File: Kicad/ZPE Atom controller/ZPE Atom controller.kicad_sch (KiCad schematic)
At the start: 44 parts, among them IC1 TC4424AVPA, J1 50 ohm 21 turns, P1 CONN_01X18, P2 CONN_01X18, Q1 2N2222, Q2 IRF3205, SW1 ON/OFF, SW2 SW_SPST, SW3 SW_SPST, SW4 SW_SPST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

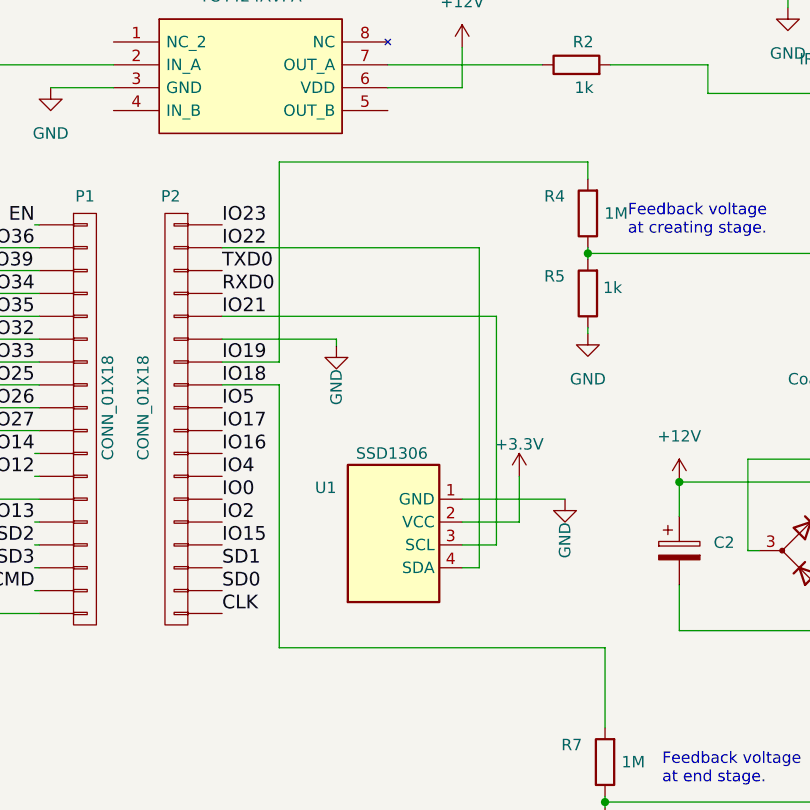
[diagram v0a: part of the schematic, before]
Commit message: Fixed analog read pin input
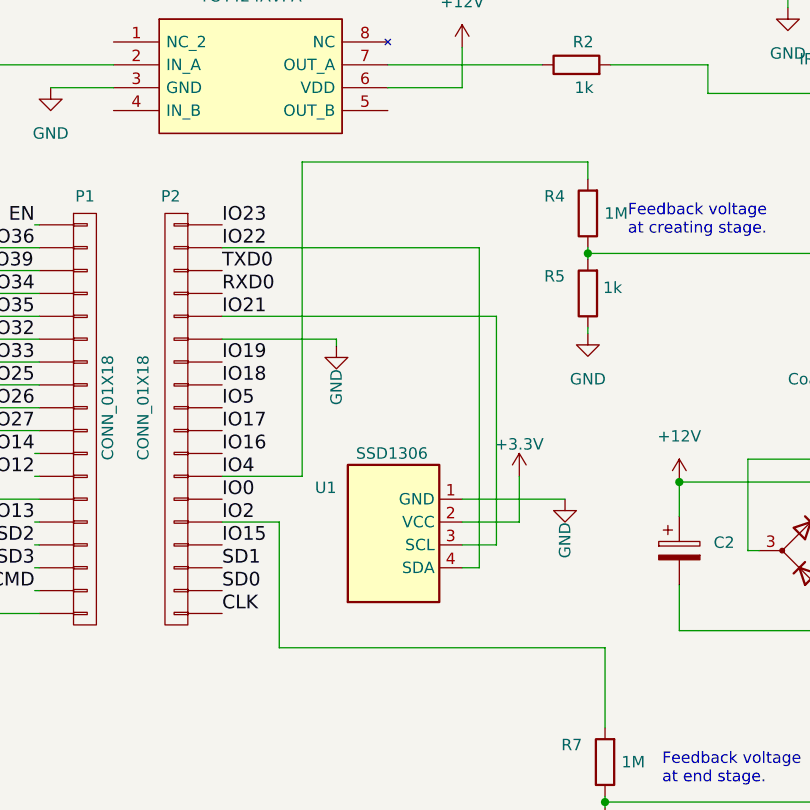
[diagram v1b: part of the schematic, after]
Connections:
- net IO18: no longer R7.2
- net IO19: no longer R4.2
- net IO2: now also R7.2
- net IO4: now also R4.2
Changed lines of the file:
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@@
+    (stroke (width 0) (type default))
+  )
+  (wire (pts (xy 86.995 113.03) (xy 93.345 113.03))
     (stroke (width 0) (type default))
   )
@@
     (stroke (width 0) (type default))
   )
-  (wire (pts (xy 86.995 97.79) (xy 93.345 97.79))
-    (stroke (width 0) (type default))
-  )
   (wire (pts (xy 113.665 110.49) (xy 125.095 110.49))
     (stroke (width 0) (type default))
@@
     (stroke (width 0) (type default))
   )
-  (wire (pts (xy 86.995 95.25) (xy 93.345 95.25))
-    (stroke (width 0) (type default))
-  )
   (wire (pts (xy 162.56 42.545) (xy 162.56 45.085))
     (stroke (width 0) (type default))
@@
     (stroke (width 0) (type default))
   )
-  (wire (pts (xy 93.345 127) (xy 93.345 97.79))
+  (wire (pts (xy 93.345 127) (xy 93.345 113.03))
     (stroke (width 0) (type default))
   )
@@
     (stroke (width 0) (type default))
   )
-  (wire (pts (xy 93.345 73.025) (xy 93.345 95.25))
+  (wire (pts (xy 95.885 73.025) (xy 95.885 107.95))
     (stroke (width 0) (type default))
   )
@@
     (stroke (width 0) (type default))
   )
-  (wire (pts (xy 127.635 73.025) (xy 93.345 73.025))
+  (wire (pts (xy 127.635 73.025) (xy 95.885 73.025))
     (stroke (width 0) (type default))
   )
@@
     (stroke (width 0) (type default))
   )
+  (wire (pts (xy 86.995 107.95) (xy 95.885 107.95))
+    (stroke (width 0) (type default))
+  )

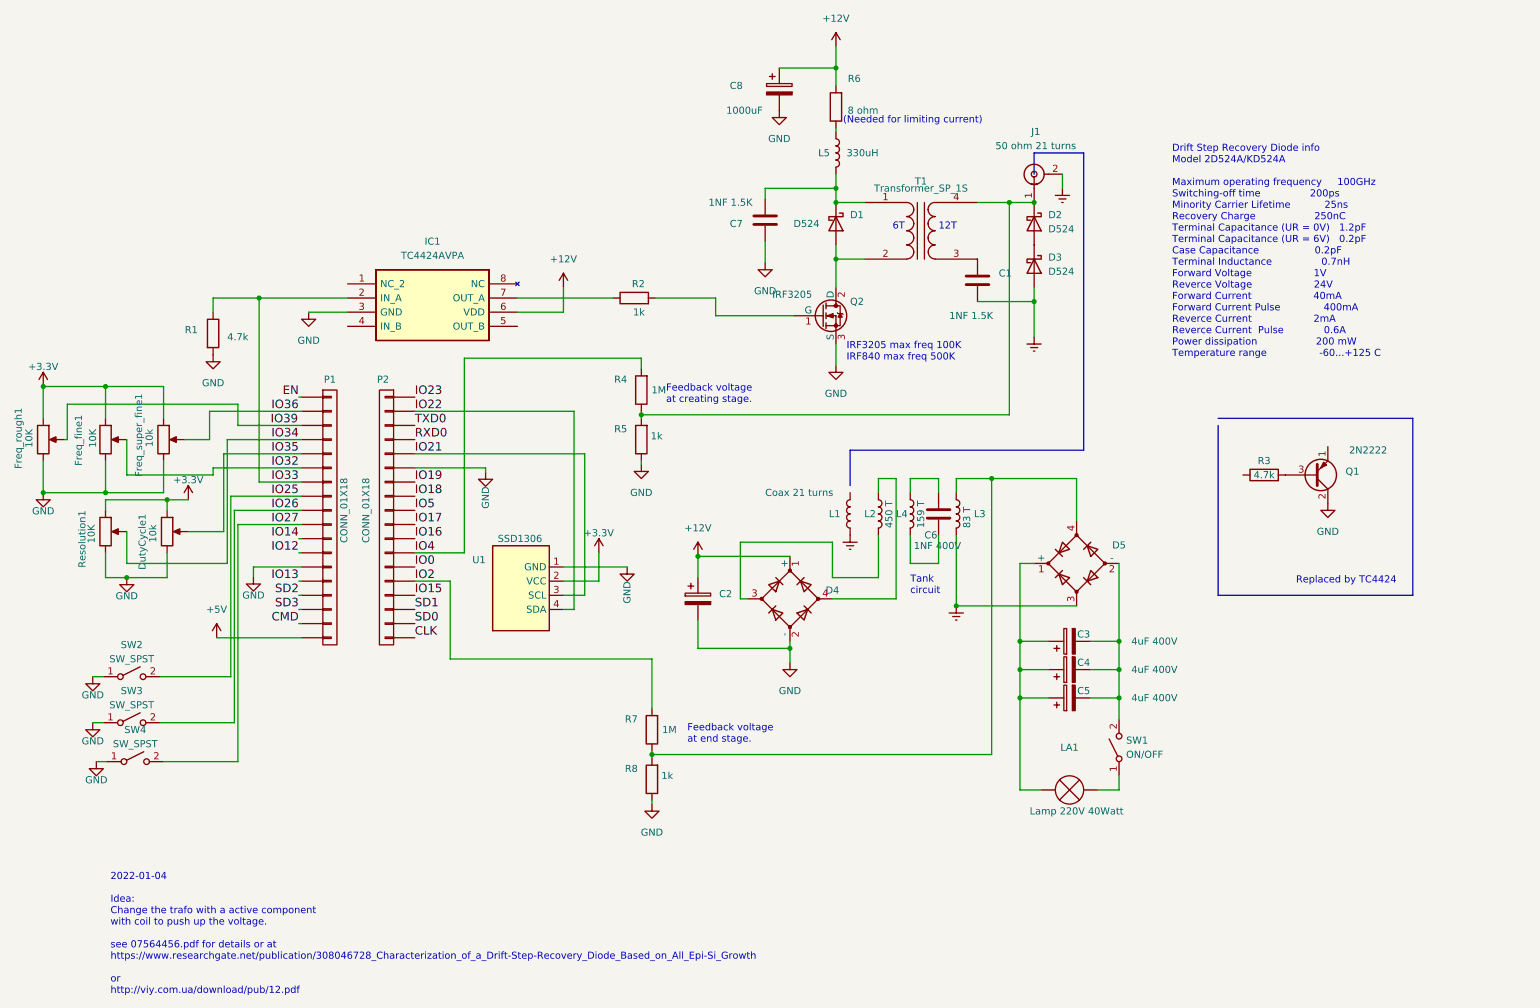
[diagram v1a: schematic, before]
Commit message: Updated schematic with current limiter
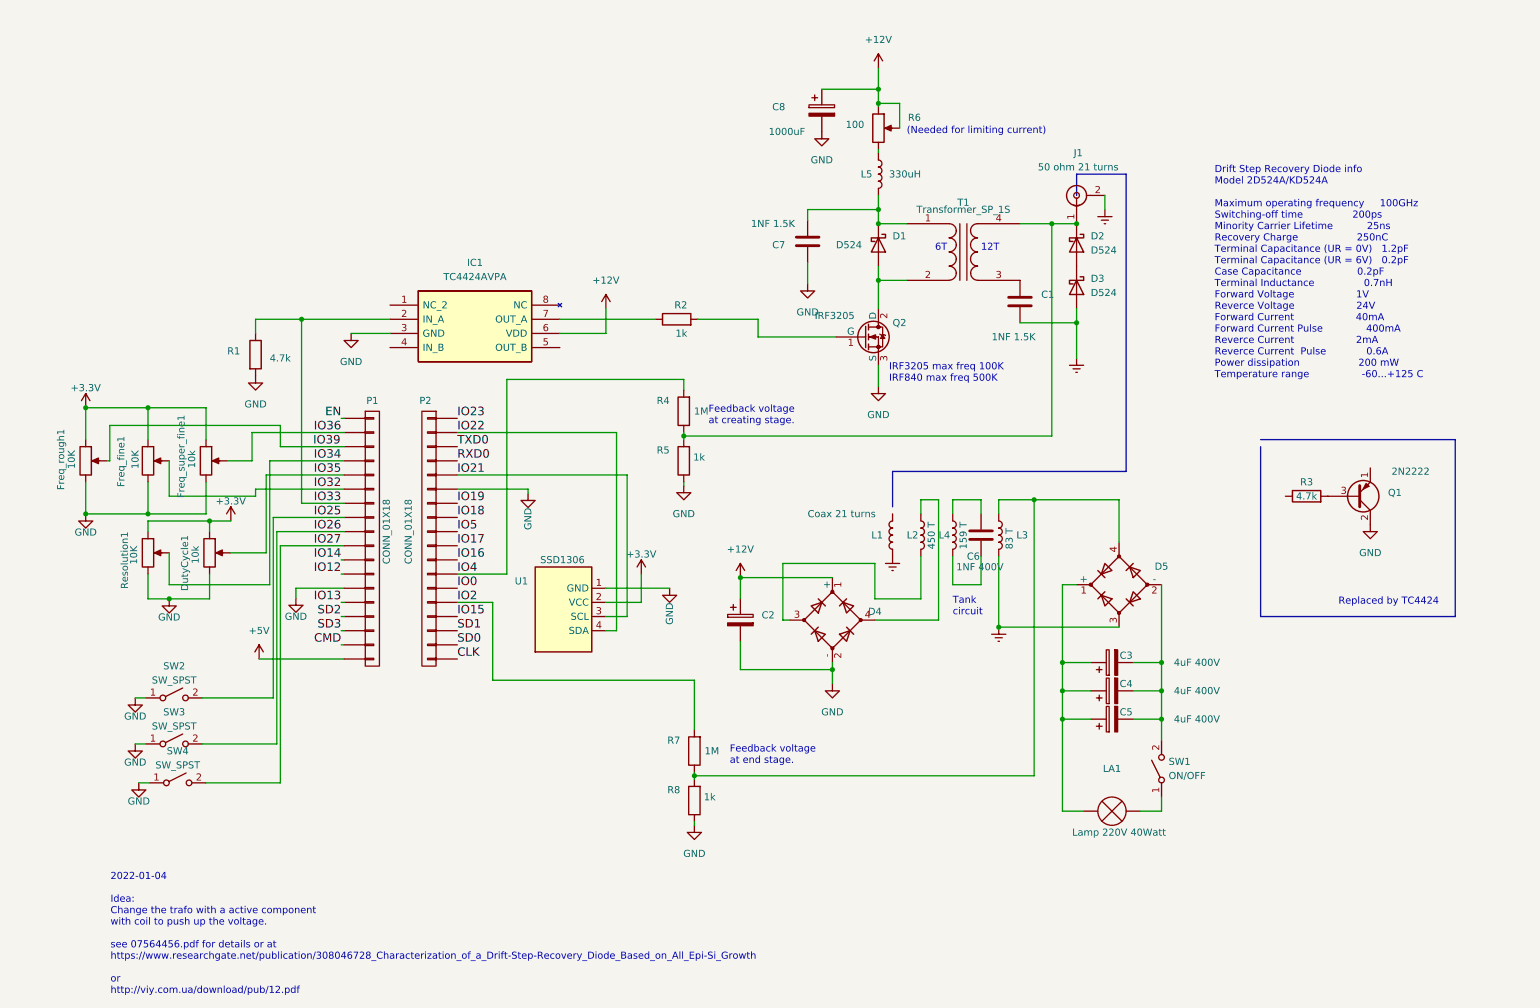
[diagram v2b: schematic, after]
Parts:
- removed R6: 8 ohm, Resistor_THT:R_Axial_DIN0207_L6.3mm_D2.5mm_P10.16mm_Horizontal, symbol Device:R
- added R6: 100, Potentiometer_THT:Potentiometer_Piher_PC-16_Single_Vertical, symbol Device:R_Potentiometer
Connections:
- net +12V: now also R6.1, R6.2
- net at L5.1: now also R6.3
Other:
- moved on the sheet: C1, C2, C3, C4, C5, C6, C7, C8, D1, D2, D3, D4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

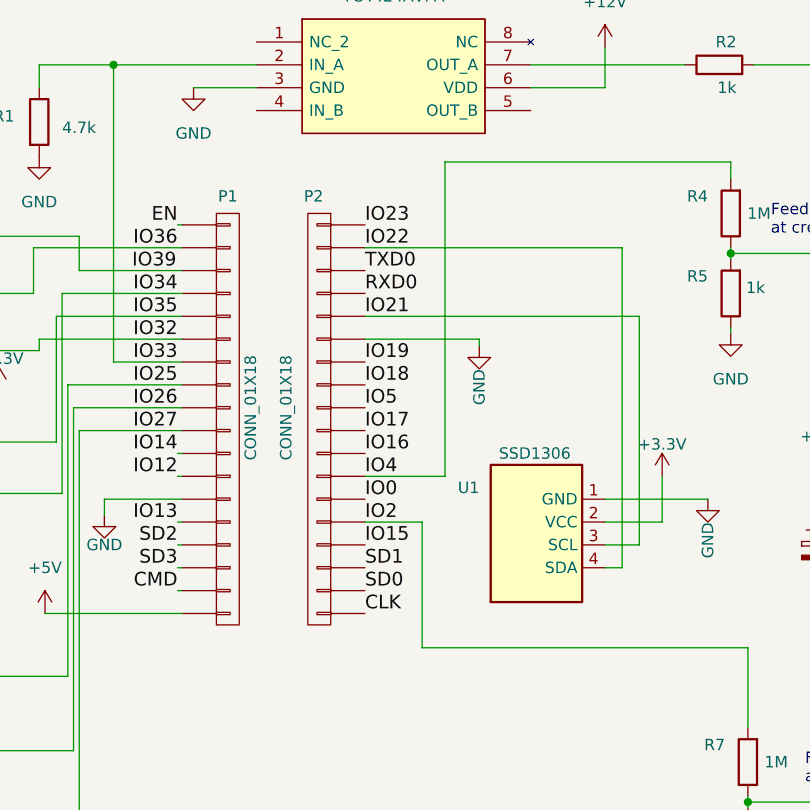
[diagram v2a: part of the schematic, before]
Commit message: Updated schematic and  code for analog input
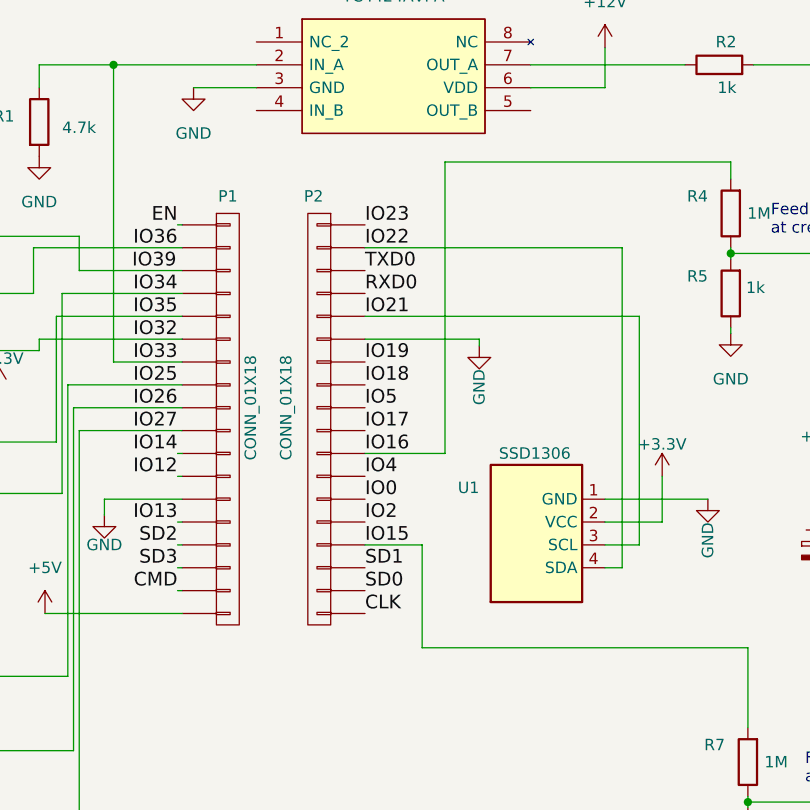
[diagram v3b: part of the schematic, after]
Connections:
- net IO15: now also R7.2
- net IO16: now also R4.2
- net IO2: no longer R7.2
- net IO4: no longer R4.2
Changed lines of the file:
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@@
-    (stroke (width 0) (type default))
-  )
-  (wire (pts (xy 94.615 116.84) (xy 100.965 116.84))
     (stroke (width 0) (type default))
   )
@@
     (stroke (width 0) (type default))
   )
+  (wire (pts (xy 103.505 109.22) (xy 94.615 109.22))
+    (stroke (width 0) (type default))
+  )
   (wire (pts (xy 27.94 81.915) (xy 39.116 81.915))
     (stroke (width 0) (type default))
@@
     (stroke (width 0) (type default))
   )
+  (wire (pts (xy 100.965 119.38) (xy 94.615 119.38))
+    (stroke (width 0) (type default))
+  )
   (wire (pts (xy 198.12 98.425) (xy 198.12 147.955))
     (stroke (width 0) (type default))
@@
     (stroke (width 0) (type default))
   )
-  (wire (pts (xy 100.965 130.81) (xy 100.965 116.84))
-    (stroke (width 0) (type default))
-  )
   (wire (pts (xy 74.295 119.38) (xy 73.787 119.38))
     (stroke (width 0) (type default))
@@
     (stroke (width 0) (type default))
   )
-  (wire (pts (xy 103.505 76.835) (xy 103.505 111.76))
+  (wire (pts (xy 103.505 76.835) (xy 103.505 109.22))
     (stroke (width 0) (type default))
   )
@@
     (stroke (width 0) (type default))
   )
-  (wire (pts (xy 94.615 111.76) (xy 103.505 111.76))
-    (stroke (width 0) (type default))
-  )
+  (wire (pts (xy 100.965 119.38) (xy 100.965 130.81))
+    (stroke (width 0) (type default))
+  )

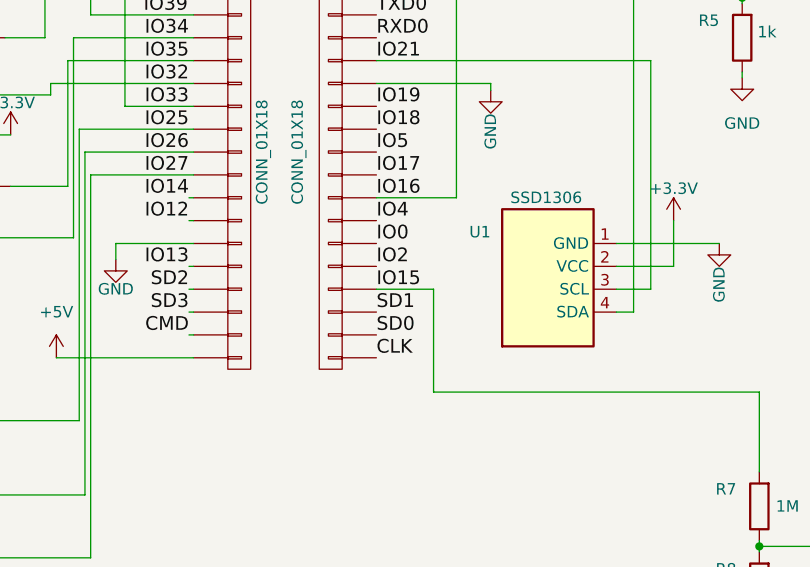
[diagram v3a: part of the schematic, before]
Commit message: Changed  pins for feedback to pin 16 and 17
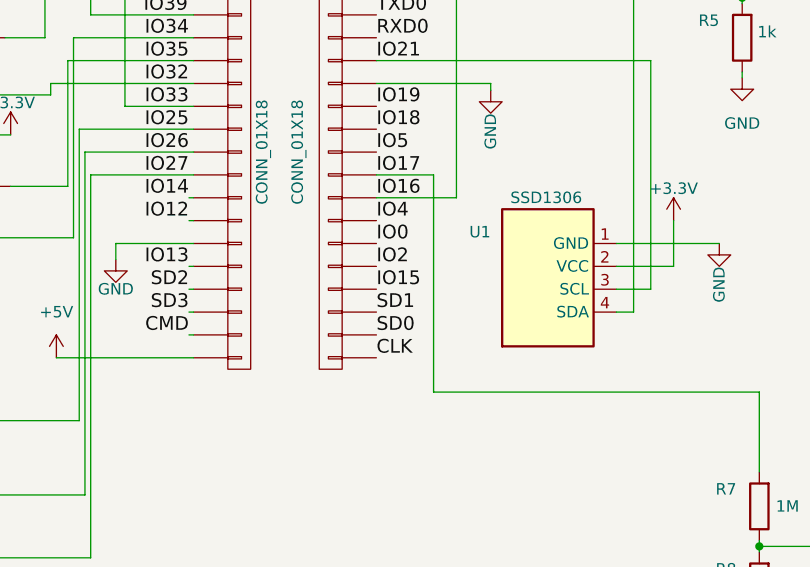
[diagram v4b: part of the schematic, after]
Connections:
- net IO15: no longer R7.2
- net IO17: now also R7.2
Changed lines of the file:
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@@
-    (stroke (width 0) (type default))
-  )
-  (wire (pts (xy 100.965 119.38) (xy 94.615 119.38))
     (stroke (width 0) (type default))
   )
@@
     (stroke (width 0) (type default))
   )
+  (wire (pts (xy 100.965 106.68) (xy 94.615 106.68))
+    (stroke (width 0) (type default))
+  )
   (polyline (pts (xy 205.74 43.815) (xy 205.74 40.005))
     (stroke (width 0) (type default))
@@
     (stroke (width 0) (type default))
   )
-  (wire (pts (xy 100.965 119.38) (xy 100.965 130.81))
-    (stroke (width 0) (type default))
-  )
+  (wire (pts (xy 100.965 106.68) (xy 100.965 130.81))
+    (stroke (width 0) (type default))
+  )
